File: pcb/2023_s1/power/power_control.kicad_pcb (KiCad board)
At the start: 2 copper layers, 21 parts, among them J1 Conn_01x05_Male, Q2 TIP122, U1 40106, U3 4N25

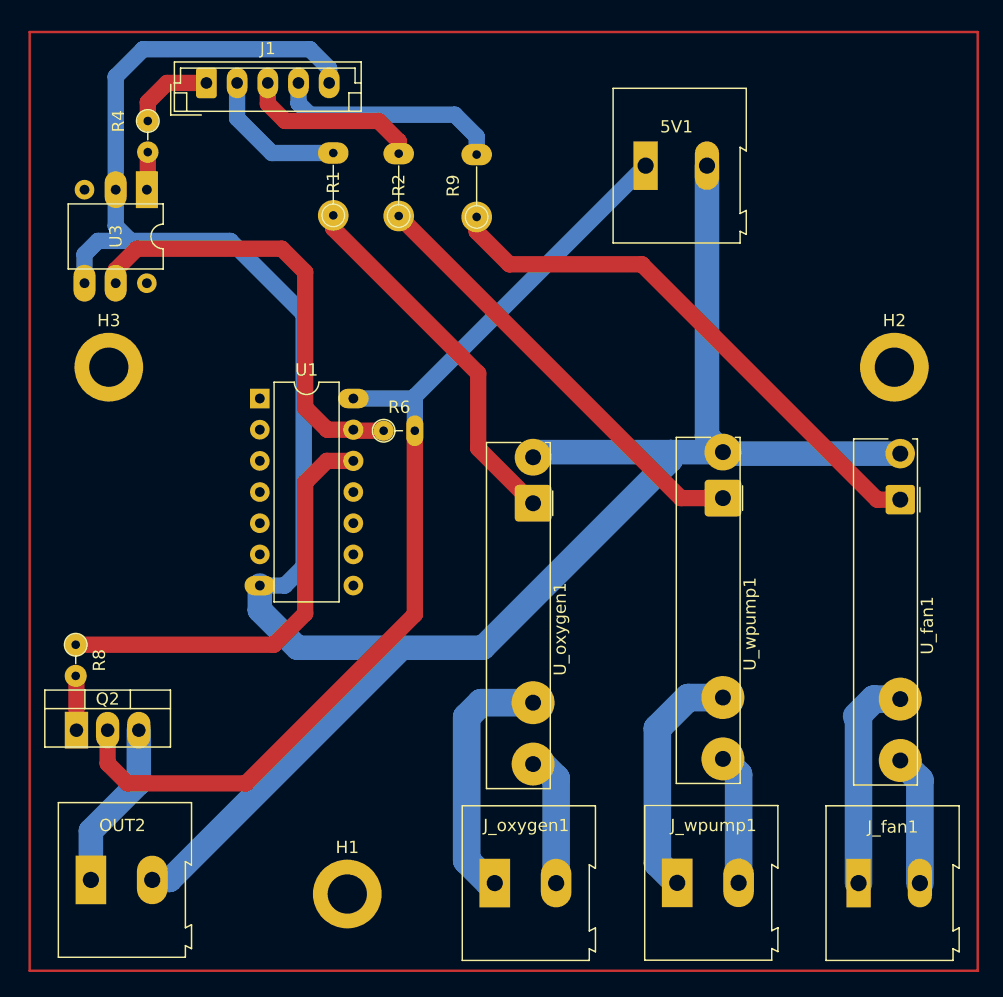
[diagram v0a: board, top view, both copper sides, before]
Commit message: fix, added a 4th mounting hole and rerouted the pcb in order to make feasible to solder given our poor infrastructure for PCB production
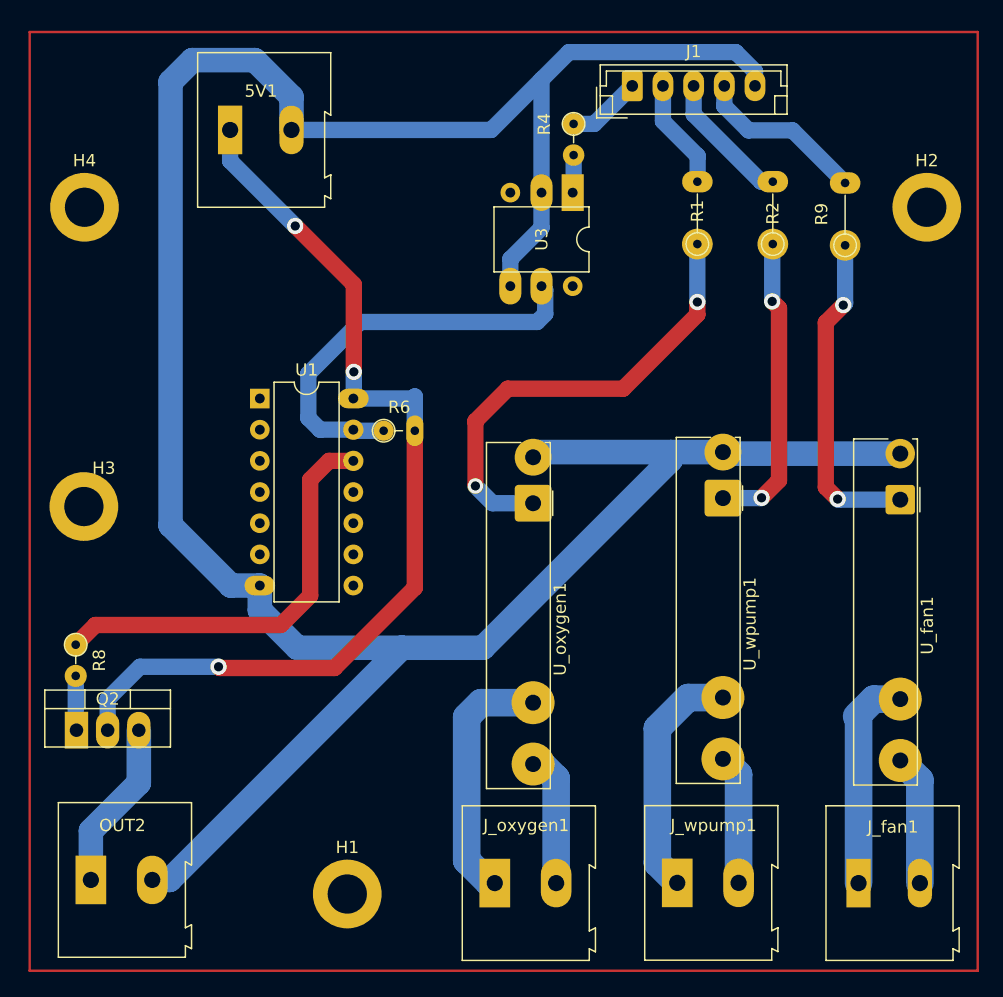
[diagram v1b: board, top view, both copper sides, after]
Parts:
- added H4: MountingHole, MountingHole:MountingHole_3.2mm_M3_DIN965_Pad, F.Cu at (131.1, 53.4)
- moved R4 34.7 mm to (171.0, 46.6)
- moved U3 34.7 mm to (170.9, 52.2)
- moved J1 34.7 mm to (175.7, 43.5)
- moved 5V1 34.0 mm to (143.0, 47.1)
- moved R2 30.6 mm to (187.2, 56.4)
- moved R9 30.1 mm to (193.1, 56.5)
- moved R1 29.8 mm to (181.1, 56.4)
- moved H2 13.3 mm to (199.7, 53.4)
- moved H3 11.5 mm to (131.1, 77.8)
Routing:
- net Net-(R9-Pad1): track 44.8 -> 26.9 mm, vias 0 -> 2
- net GND5V: track 208.2 -> 222.4 mm
- net Net-(R2-Pad1): track 35.9 -> 24.7 mm, vias 0 -> 2
- net Net-(R1-Pad1): track 30.2 -> 38.0 mm, vias 0 -> 2
- net 5v: track 83.6 -> 78.2 mm, vias 0 -> 3
- net D34: track 18.8 -> 14.1 mm
- net D33: track 14.6 -> 11.0 mm
- net D32: track 11.9 -> 8.99 mm
- net Net-(R6-Pad1): track 36.2 -> 34.0 mm
- net D25: track 6.96 -> 6.06 mm
- net Net-(R8-Pad1): track 35.1 -> 34.4 mm

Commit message: fix, changed small naming
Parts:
- moved 5V1 4.90 mm to (147.9, 47.1), turned to 180 degrees
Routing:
- net GND5V: track 222.4 -> 212.2 mm
- net 5v: track 78.2 -> 76.2 mm
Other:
- board text added: "5V+"
- board text added: "AC"
- board text added: "GND5V"
- board text added: "INPUT"
- board text added: "OUT"
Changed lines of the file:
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@@
     (fp_line (start 12.5 -1.6) (end -2.5 -1.6) (layer "F.Fab") (width 0.1))
     (fp_line (start -2.91 0.11) (end -2.91 2.61) (layer "F.Fab") (width 0.1))
-    (pad "1" thru_hole roundrect (at 0 0) (size 1.7 2.5) (drill 0.95) (layers *.Cu *.Mask) (roundrect_rratio 0.147059)
+    (pad "1" thru_hole roundrect (at 0 0) (size 1.7 2.5) (drill 0.95) (layers *.Cu *.Mask) (roundrect_rratio 0.1470588235)
       (net 2 "D25") (pinfunction "Pin_1") (pintype "passive"))
     (pad "2" thru_hole oval (at 2.5 0) (size 1.7 2.5) (drill 0.95) (layers *.Cu *.Mask)
@@
   )
   (footprint "TerminalBlock:TerminalBlock_Altech_AK300-2_P5.00mm" (layer "F.Cu")
-    (at 142.9802 47.0916)
+    (at 147.8788 47.0916 180)
     (descr "Altech AK300 terminal block, pitch 5.0mm, 45 degree angled, see http://www.mouser.com/ds/2/16/PCBMETRC-24178.pdf")
     (tags "Altech AK300 terminal block pitch 5.0mm")
@@
     (fp_arc (start 6.54 -5.05) (mid 6.715733 -4.551652) (end 6.485532 -4.076005) (layer "F.Fab") (width 0.1))
     (fp_arc (start -1.62 -5) (mid -0.05669 -5.772528) (end 1.539976 -5.071534) (layer "F.Fab") (width 0.1))
-    (pad "1" thru_hole rect (at 0 0) (size 1.98 3.96) (drill 1.32) (layers *.Cu *.Mask)
+    (pad "1" thru_hole rect (at 0 0 180) (size 1.98 3.96) (drill 1.32) (layers *.Cu *.Mask)
       (net 11 "5v") (pinfunction "Pin_1") (pintype "passive"))
-    (pad "2" thru_hole oval (at 5 0) (size 1.98 3.96) (drill 1.32) (layers *.Cu *.Mask)
+    (pad "2" thru_hole oval (at 5 0 180) (size 1.98 3.96) (drill 1.32) (layers *.Cu *.Mask)
       (net 1 "GND5V") (pinfunction "Pin_2") (pintype "passive"))
     (model "${KICAD6_3DMODEL_DIR}/TerminalBlock.3dshapes/TerminalBlock_Altech_AK300-2_P5.00mm.wrl"
@@
   )
   (gr_rect (start 203.894 39.111) (end 126.647 115.6) (layer "F.Cu") (width 0.2) (fill none))
-  (segment (start 147.9802 44.399) (end 147.9802 47.0916) (width 2) (layer "B.Cu") (net 1))
+  (gr_text "GND5V\n" (at 135.7884 46.6852) (layer "F.Cu")
+    (effects (font (size 1.5 1.5) (thickness 0.3)))
+  )
+  (gr_text "AC" (at 174.8536 109.982) (layer "F.Cu")
+    (effects (font (size 1.5 1.5) (thickness 0.3) italic))
+  )
+  (gr_text "GND5V\n" (at 141.478 111.252 90) (layer "F.Cu")
+    (effects (font (size 1.5 1.5) (thickness 0.3)))
+  )
+  (gr_text "AC" (at 158.3944 109.982) (layer "F.Cu")
+    (effects (font (size 1.5 1.5) (thickness 0.3) italic))
+  )
+  (gr_text "OUT" (at 134.5692 100.6856) (layer "F.Cu")
+    (effects (font (size 1.5 1.5) (thickness 0.3) italic))
+  )
+  (gr_text "AC" (at 189.6364 109.982) (layer "F.Cu")
+    (effects (font (size 1.5 1.5) (thickness 0.3) italic))
+  )
+  (gr_text "INPUT" (at 135.4836 41.6052) (layer "F.Cu")
+    (effects (font (size 1.5 1.5) (thickness 0.3) italic))
+  )
+  (gr_text "5V+" (at 127.8636 112.1664 90) (layer "F.Cu")
+    (effects (font (size 1.5 1.5) (thickness 0.3) italic))
+  )
+  (gr_text "5V+" (at 153.162 46.9392) (layer "F.Cu")
+    (effects (font (size 1.5 1.5) (thickness 0.3)))
+  )
+  (gr_text "GND5V\n" (at 192.9892 43.8404) (layer "F.Cu")
+    (effects (font (size 1.5 1.5) (thickness 0.3)))
+  )
   (segment (start 178.876 73.339) (end 178.876 73.981) (width 2) (layer "B.Cu") (net 1))
   (segment (start 183.261 73.466) (end 183.134 73.339) (width 2) (layer "B.Cu") (net 1))
   (segment (start 178.876 73.339) (end 168.0865 73.339) (width 2) (layer "B.Cu") (net 1))
-  (segment (start 168.3524 42.9861) (end 164.2469 47.0916) (width 1.33) (layer "B.Cu") (net 1))
+  (segment (start 145.4 84.215) (end 143.0414 84.215) (width 2) (layer "B.Cu") (net 1))
   (segment (start 184.1754 40.7521) (end 170.5864 40.7521) (width 1.33) (layer "B.Cu") (net 1))
   (segment (start 168.0865 73.339) (end 167.6675 73.758) (width 2) (layer "B.Cu") (net 1))
   (segment (start 145.4 86.218) (end 148.463 89.281) (width 2) (layer "B.Cu") (net 1))
+  (segment (start 146.2532 42.418) (end 142.8788 45.7924) (width 1.33) (layer "B.Cu") (net 1))
   (segment (start 197.583 73.466) (end 183.261 73.466) (width 2) (layer "B.Cu") (net 1))
+  (segment (start 167.7843 42.418) (end 146.2532 42.418) (width 1.33) (layer "B.Cu") (net 1))
+  (segment (start 138.1252 51.8452) (end 142.8788 47.0916) (width 2) (layer "B.Cu") (net 1))
   (segment (start 168.3524 42.9861) (end 168.3524 52.1981) (width 1.33) (layer "B.Cu") (net 1))
+  (segment (start 142.8788 45.7924) (end 142.8788 47.0916) (width 1.33) (layer "B.Cu") (net 1))
   (segment (start 183.134 73.339) (end 178.876 73.339) (width 2) (layer "B.Cu") (net 1))
-  (segment (start 143.0414 84.215) (end 138.1252 79.2988) (width 2) (layer "B.Cu") (net 1))
-  (segment (start 138.1252 79.2988) (end 138.1252 43.18) (width 2) (layer "B.Cu") (net 1))
+  (segment (start 138.1252 79.2988) (end 138.1252 51.8452) (width 2) (layer "B.Cu") (net 1))
   (segment (start 185.7464 42.3231) (end 184.1754 40.7521) (width 1.33) (layer "B.Cu") (net 1))
   (segment (start 163.576 89.281) (end 156.972 89.281) (width 2) (layer "B.Cu") (net 1))
   (segment (start 170.5864 40.7521) (end 168.3524 42.9861) (width 1.33) (layer "B.Cu") (net 1))
-  (segment (start 139.9032 41.402) (end 144.9832 41.402) (width 2) (layer "B.Cu") (net 1))
   (segment (start 165.8124 57.606) (end 168.3524 55.066) (width 1.33) (layer "B.Cu") (net 1))
   (segment (start 145.4 84.215) (end 145.4 86.218) (width 2) (layer "B.Cu") (net 1))
+  (segment (start 168.3524 42.9861) (end 167.7843 42.418) (width 1.33) (layer "B.Cu") (net 1))
   (segment (start 136.635 108.2) (end 138.053 108.2) (width 2) (layer "B.Cu") (net 1))
   (segment (start 167.4675 73.558) (end 167.6675 73.758) (width 1.85) (layer "B.Cu") (net 1))
   (segment (start 178.876 73.981) (end 163.576 89.281) (width 2) (layer "B.Cu") (net 1))
-  (segment (start 164.2469 47.0916) (end 147.9802 47.0916) (width 1.33) (layer "B.Cu") (net 1))
-  (segment (start 145.4 84.215) (end 143.0414 84.215) (width 2) (layer "B.Cu") (net 1))
   (segment (start 138.053 108.2) (end 156.972 89.281) (width 2) (layer "B.Cu") (net 1))
   (segment (start 156.972 89.281) (end 148.463 89.281) (width 2) (layer "B.Cu") (net 1))
-  (segment (start 138.1252 43.18) (end 139.9032 41.402) (width 2) (layer "B.Cu") (net 1))
   (segment (start 165.8124 59.8181) (end 165.8124 57.606) (width 1.33) (layer "B.Cu") (net 1))
-  (segment (start 144.9832 41.402) (end 147.9802 44.399) (width 2) (layer "B.Cu") (net 1))
+  (segment (start 143.0414 84.215) (end 138.1252 79.2988) (width 2) (layer "B.Cu") (net 1))
   (segment (start 185.7464 43.5001) (end 185.7464 42.3231) (width 1.33) (layer "B.Cu") (net 1))
   (segment (start 168.3524 55.066) (end 168.3524 52.1981) (width 1.33) (layer "B.Cu") (net 1))
@@
   (via (at 153.0604 66.802) (size 1.33) (drill 0.75) (layers "F.Cu" "B.Cu") (net 11))
   (via (at 148.2852 54.9148) (size 1.33) (drill 0.75) (layers "F.Cu" "B.Cu") (net 11))
-  (segment (start 142.9802 47.0916) (end 142.9802 49.6098) (width 1.33) (layer "B.Cu") (net 11))
+  (segment (start 147.8788 54.5084) (end 148.2852 54.9148) (width 1.33) (layer "B.Cu") (net 11))
   (segment (start 158.03 68.805) (end 157.86 68.975) (width 1.33) (layer "B.Cu") (net 11))
   (segment (start 142.0368 90.8304) (end 135.636 90.8304) (width 1.33) (layer "B.Cu") (net 11))
@@
   (segment (start 133 93.4664) (end 133 96) (width 1.33) (layer "B.Cu") (net 11))
   (segment (start 135.636 90.8304) (end 133 93.4664) (width 1.33) (layer "B.Cu") (net 11))
+  (segment (start 147.8788 47.0916) (end 147.8788 54.5084) (width 1.33) (layer "B.Cu") (net 11))
   (segment (start 153.0604 66.802) (end 153.0604 68.9346) (width 1.33) (layer "B.Cu") (net 11))
   (segment (start 157.86 68.975) (end 153.02 68.975) (width 1.33) (layer "B.Cu") (net 11))
-  (segment (start 142.9802 49.6098) (end 148.2852 54.9148) (width 1.33) (layer "B.Cu") (net 11))
   (segment (start 181.0512 62.1284) (end 175.006 68.1736) (width 1.33) (layer "F.Cu") (net 12))
   (segment (start 165.608 68.1736) (end 162.9664 70.8152) (width 1.33) (layer "F.Cu") (net 12))

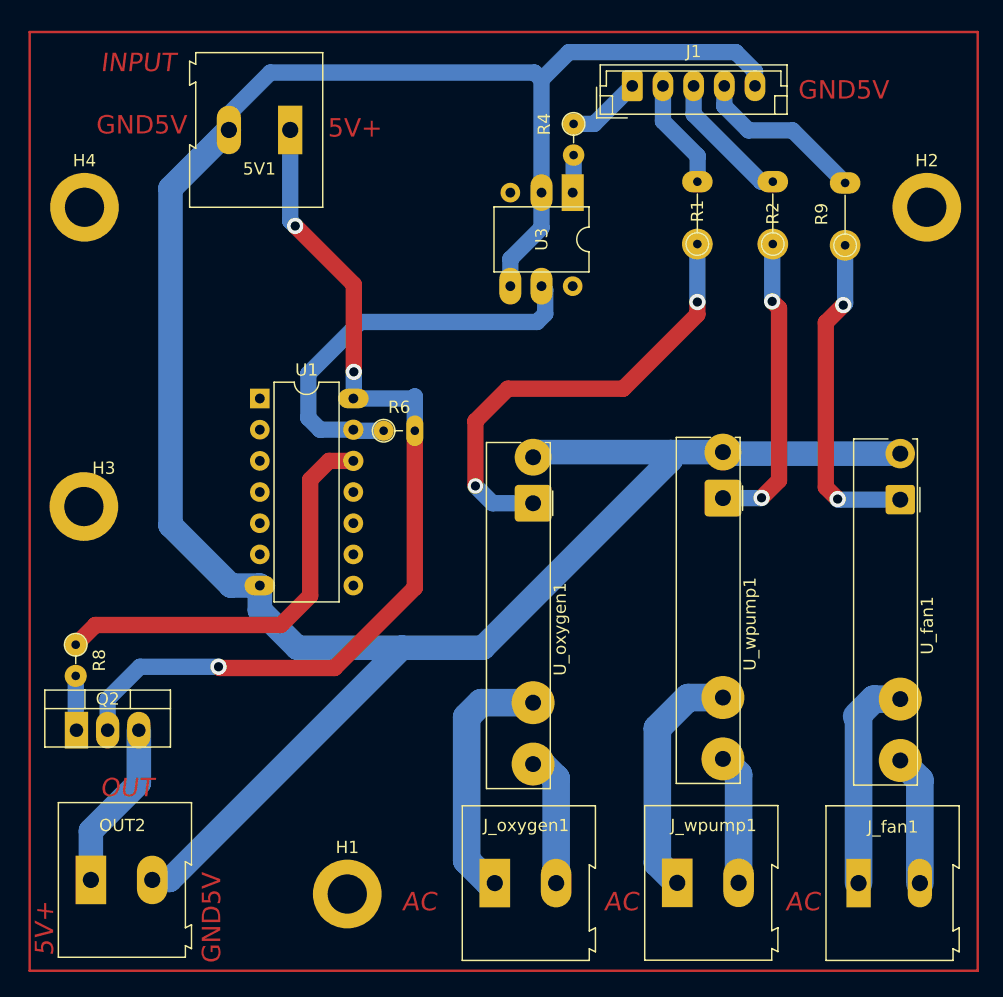
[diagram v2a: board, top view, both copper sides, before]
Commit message: update, reselection of output pins and ds18b20 pin, rerouting and resizing of pads
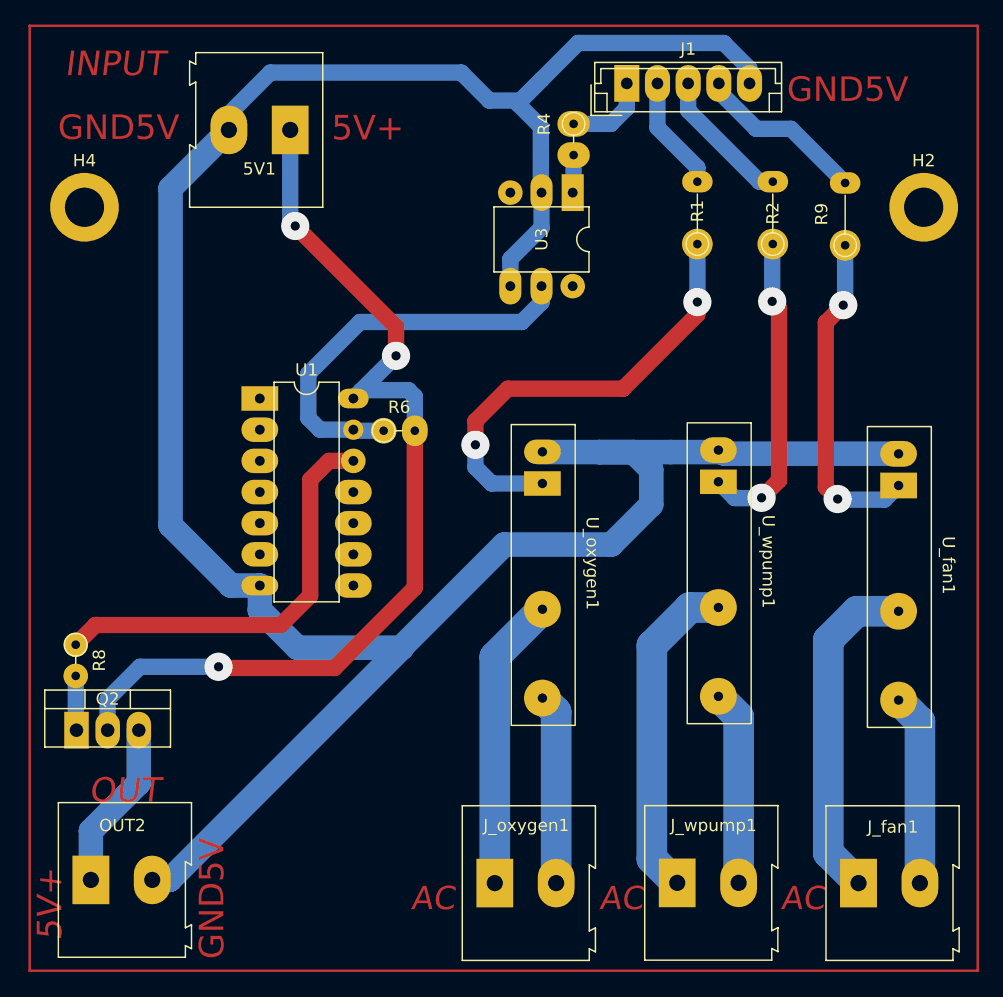
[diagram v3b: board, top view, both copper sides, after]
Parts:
- removed H1, H3: MountingHole, MountingHole:MountingHole_3.2mm_M3_DIN965_Pad
- U_fan1, U_oxygen1, U_wpump1: footprint OptoDevice:Finder_34.81 -> smart_sensor:G3MB-202P
- moved U_fan1 5.35 mm to (197.3, 82.6)
- moved U_wpump1 5.19 mm to (182.6, 82.3)
- moved U_oxygen1 4.93 mm to (168.3, 82.4)
- moved J1 0.49 mm to (175.3, 43.3)
- moved H2 0.25 mm to (199.5, 53.4)
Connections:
- net D25 renamed D14
- net D32 renamed D26
- J1 pad 3: D33 -> D27
- J1 pad 4: D34 -> D33
- R2 pad 2: D33 -> D27
- R9 pad 2: D34 -> D33
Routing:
- net D34: track 14.1 -> 0.00 mm
- net D27: track 0.00 -> 11.5 mm
- net Net-(J_fan1-Pad1): track 17.8 -> 27.5 mm
- net Net-(J_wpump1-Pad1): track 19.6 -> 27.0 mm
- net GND5V: track 212.2 -> 218.5 mm
- net Net-(J_wpump1-Pad2): track 10.6 -> 15.9 mm
- net Net-(J_fan1-Pad2): track 10.7 -> 15.6 mm
- net Net-(J_oxygen1-Pad2): track 10.9 -> 15.5 mm
- net Net-(J_oxygen1-Pad1): track 20.6 -> 23.9 mm
- net 5v: track 76.2 -> 79.4 mm
- net D33: track 11.0 -> 14.0 mm
- net Net-(R6-Pad1): track 34.0 -> 33.0 mm
- net Net-(R2-Pad1): track 24.7 -> 25.7 mm
- net D14: track 6.06 -> 6.87 mm
- net Net-(R1-Pad1): track 38.0 -> 37.2 mm

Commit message: update, new export files and added voltage elevator space for lights control pcb
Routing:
- net GND5V: track 218.5 -> 220.8 mm
- net Net-(R8-Pad1): track 34.4 -> 35.2 mm, vias 0 -> 2
- net 5v: vias 3 -> 4
